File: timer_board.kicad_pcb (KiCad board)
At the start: 2 copper layers, 139.7 x 88.9 mm, 59 parts, among them CON1 AVR-ISP-6, IC1 ATMEGA32U4, K1 T9AS5D22-5, P1 USBMICRO, P2 OUT_INV, P3 Trigger, P4 OUT, P5 ADC, P6 32Khz, Q1 NPN, Q2 NPN, U1 DS3231MZ, U2 74HC04, Y1 RESONATORSMD

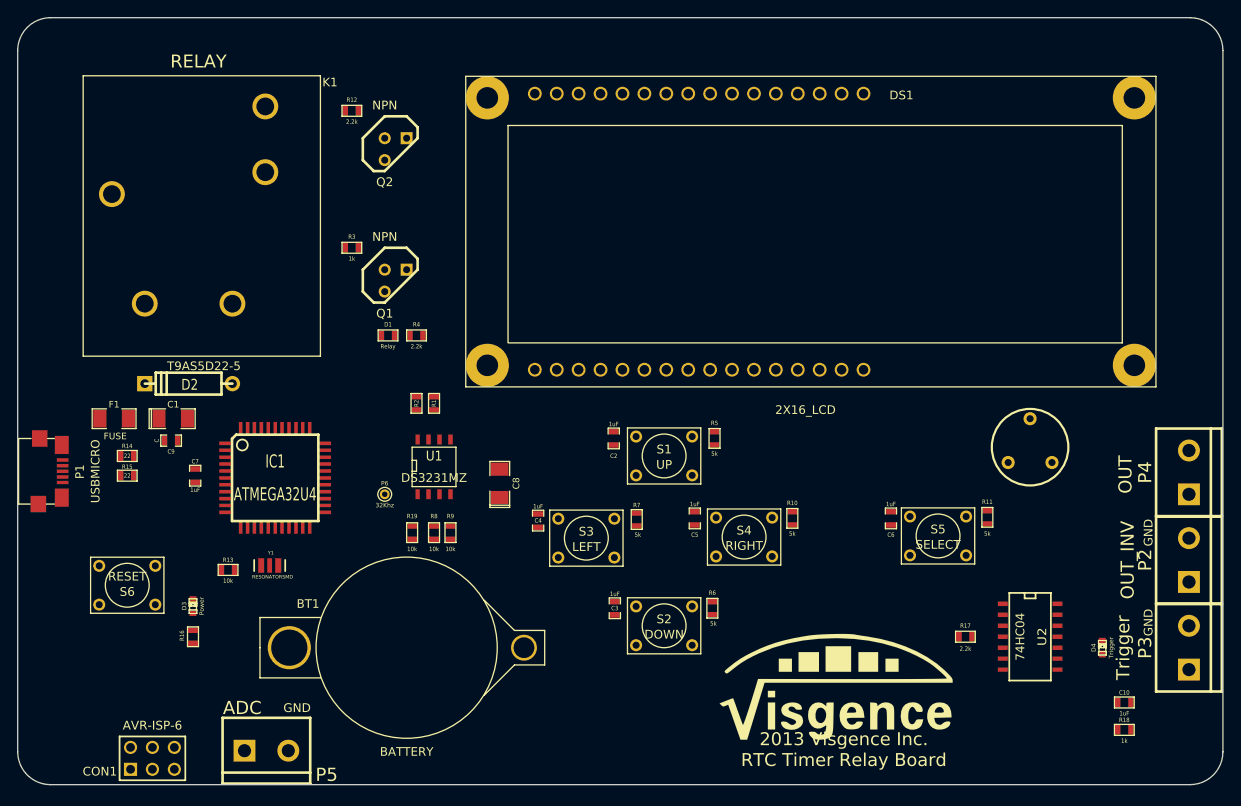
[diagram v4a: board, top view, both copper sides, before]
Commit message: Added mounting holes
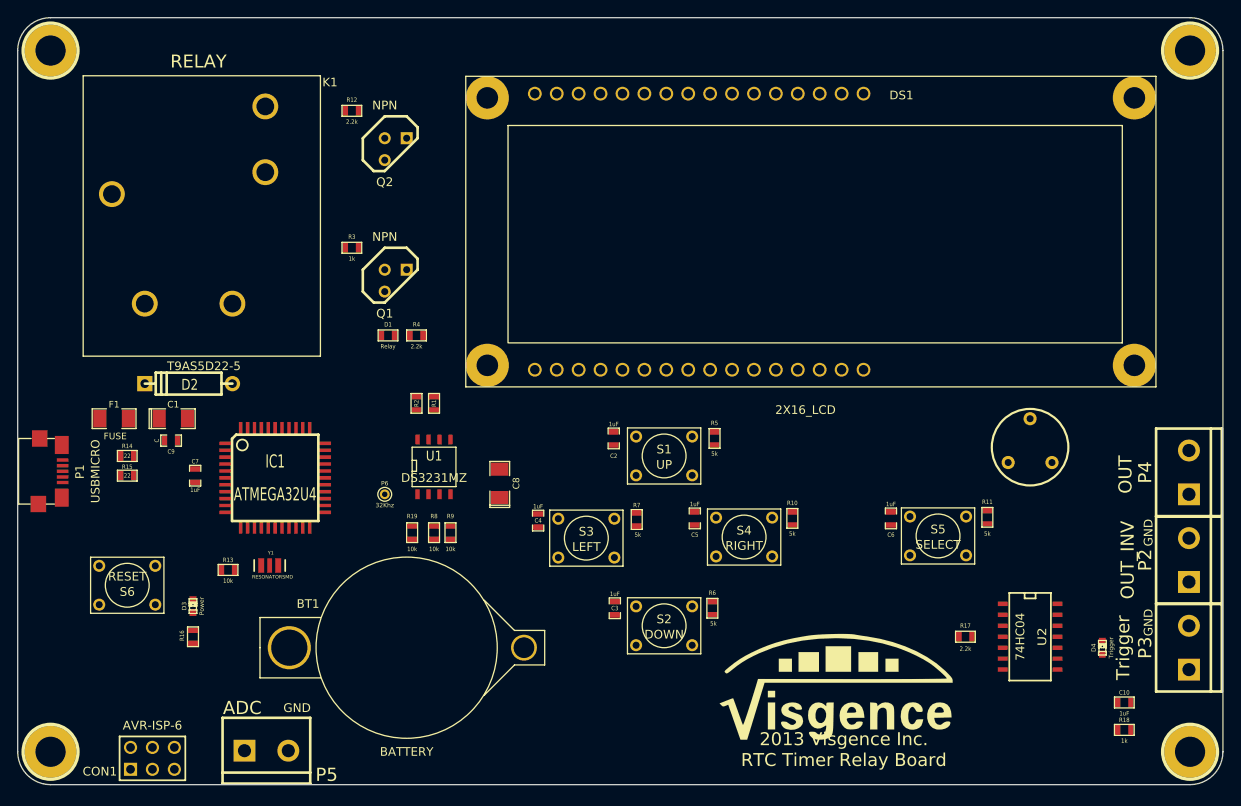
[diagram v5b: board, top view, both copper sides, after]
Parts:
- added p10: pin, 1pin_C, F.Cu at (29.2, 29.2)
- added p11: pin, 1pin_C, F.Cu at (29.2, 110.5)
- added p12: pin, 1pin_C, F.Cu at (161.3, 29.2)
- added p13: pin, 1pin_C, F.Cu at (161.3, 110.5)
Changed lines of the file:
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@@
 (kicad_pcb (version 3) (host pcbnew "(2013-07-07 BZR 4022)-stable")
   (general
-    (links 233)
+    (links 0)
     (no_connects 161)
-    (area 25.349999 25.349999 165.150001 114.350001)
+    (area 25.177999 25.349999 165.379401 114.579401)
     (thickness 1.6)
     (drawings 14)
     (tracks 0)
     (zones 0)
-    (modules 59)
+    (modules 63)
     (nets 50)
   )
@@
     )
   )
+  (module 1pin_C (layer F.Cu)
+    (at 29.21 29.21)
+    (descr "module 1 pin (ou trou mecanique de percage)")
+    (tags DEV)
+    (path 1pin)
+    (fp_text reference p10 (at 0 -3.048) (layer F.SilkS) hide
+      (effects (font (size 1.016 1.016) (thickness 0.254)))
+    )
+    (fp_text value pin (at 0 2.794) (layer F.SilkS) hide
+      (effects (font (size 1.016 1.016) (thickness 0.254)))
+    )
+    (fp_circle (center 0 0) (end 3.175 0.2286) (layer F.SilkS) (width 0.381))
+    (pad 1 thru_hole circle (at 0 0) (size 6 6) (drill 3.5)
+      (layers *.Cu *.Mask F.SilkS)
+    )
+  )
+  (module 1pin_C (layer F.Cu)
+    (at 29.21 110.49)
+    (descr "module 1 pin (ou trou mecanique de percage)")
+    (tags DEV)
+    (path 1pin)
+    (fp_text reference p11 (at 0 -3.048) (layer F.SilkS) hide
+      (effects (font (size 1.016 1.016) (thickness 0.254)))
+    )
+    (fp_text value pin (at 0 2.794) (layer F.SilkS) hide
+      (effects (font (size 1.016 1.016) (thickness 0.254)))
+    )
+    (fp_circle (center 0 0) (end 3.175 0.2286) (layer F.SilkS) (width 0.381))
+    (pad 1 thru_hole circle (at 0 0) (size 6 6) (drill 3.5)
+      (layers *.Cu *.Mask F.SilkS)
+    )
+  )
+  (module 1pin_C (layer F.Cu)
+    (at 161.29 29.21)
+    (descr "module 1 pin (ou trou mecanique de percage)")
+    (tags DEV)
+    (path 1pin)
+    (fp_text reference p12 (at 0 -3.048) (layer F.SilkS) hide
+      (effects (font (size 1.016 1.016) (thickness 0.254)))
+    )
+    (fp_text value pin (at 0 2.794) (layer F.SilkS) hide
+      (effects (font (size 1.016 1.016) (thickness 0.254)))
+    )
+    (fp_circle (center 0 0) (end 3.175 0.2286) (layer F.SilkS) (width 0.381))
+    (pad 1 thru_hole circle (at 0 0) (size 6 6) (drill 3.5)
+      (layers *.Cu *.Mask F.SilkS)
+    )
+  )
+  (module 1pin_C (layer F.Cu)
+    (at 161.29 110.49)
+    (descr "module 1 pin (ou trou mecanique de percage)")
+    (tags DEV)
+    (path 1pin)
+    (fp_text reference p13 (at 0 -3.048) (layer F.SilkS) hide
+      (effects (font (size 1.016 1.016) (thickness 0.254)))
+    )
+    (fp_text value pin (at 0 2.794) (layer F.SilkS) hide
+      (effects (font (size 1.016 1.016) (thickness 0.254)))
+    )
+    (fp_circle (center 0 0) (end 3.175 0.2286) (layer F.SilkS) (width 0.381))
+    (pad 1 thru_hole circle (at 0 0) (size 6 6) (drill 3.5)
+      (layers *.Cu *.Mask F.SilkS)
+    )
+  )

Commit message: Routed board
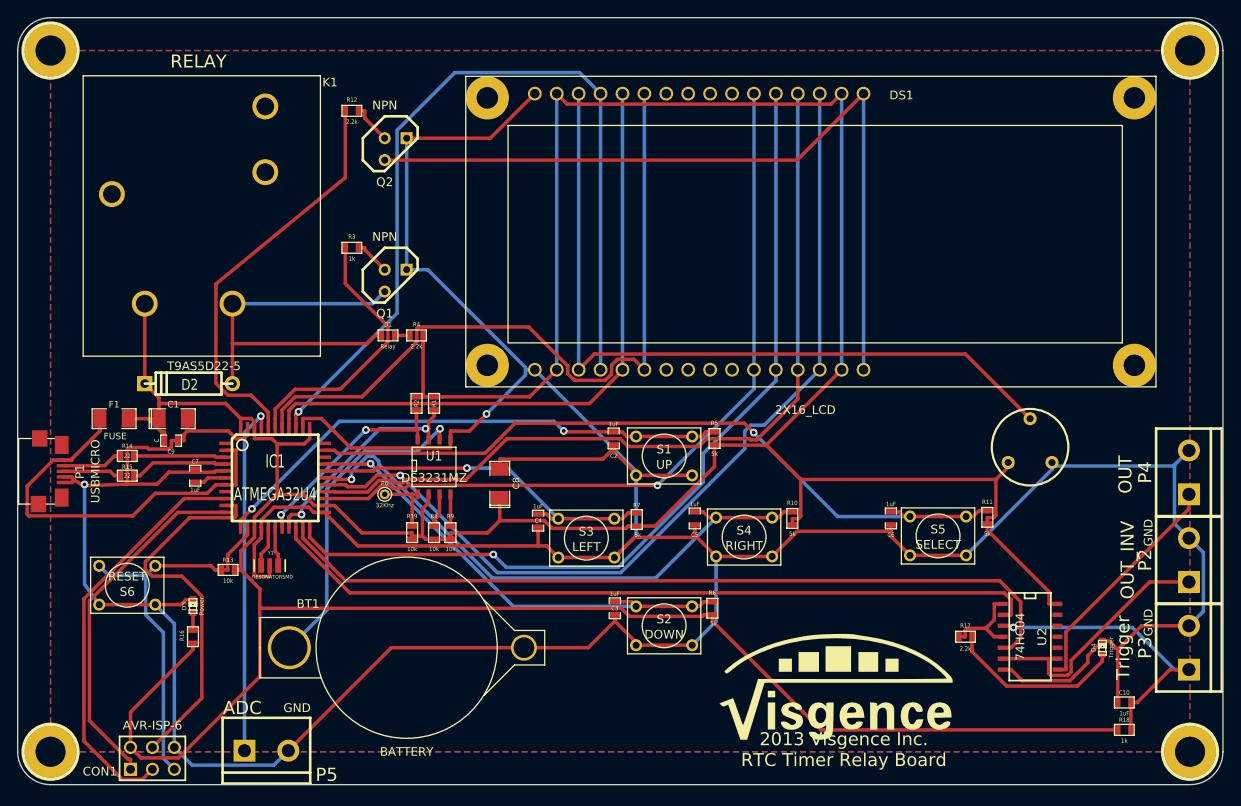
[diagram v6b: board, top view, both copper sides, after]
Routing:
- net GND: track 0.00 -> 495.8 mm, vias 0 -> 2
- net +5V: track 0.00 -> 480.4 mm
- net DB7: track 0.00 -> 105.7 mm, vias 0 -> 1
- net DB5: track 0.00 -> 100.8 mm, vias 0 -> 1
- net RS: track 0.00 -> 98.8 mm, vias 0 -> 1
- net DB6: track 0.00 -> 95.8 mm
- net OUT: track 0.00 -> 94.3 mm
- net N-000005: track 0.00 -> 90.7 mm
- net N-000002: track 0.00 -> 89.9 mm
- net DB4: track 0.00 -> 89.5 mm, vias 0 -> 1
- net N-000046: track 0.00 -> 88.2 mm
- net E: track 0.00 -> 86.2 mm
- net Select: track 0.00 -> 85.6 mm, vias 0 -> 1
- net RW: track 0.00 -> 74.8 mm
- net Right: track 0.00 -> 67.9 mm, vias 0 -> 1
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- added copper zone on B.Cu, net GND
- added copper zone on F.Cu, net GND
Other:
- net class Default: clearance 0.254 -> 0.2032; trace_width 0.254 -> 0.4064
- rule pad_to_mask_clearance: 0 -> 0.0254
- rule trace_clearance: 0.254 -> 0.2032
